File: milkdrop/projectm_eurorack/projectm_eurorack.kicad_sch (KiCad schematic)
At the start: 59 parts, among them J1 Micro_SD_Card, J2 Barrel_Jack_Switch, J2 Conn_02x05_Odd_Even, J3 AudioJack3_SwitchT, J4 USB_A, J5 AudioJack3_SwitchT, J6 690-019-298-412, Q1 MMBT3904, SW1 SW_Push, U1 RT9742SNGV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

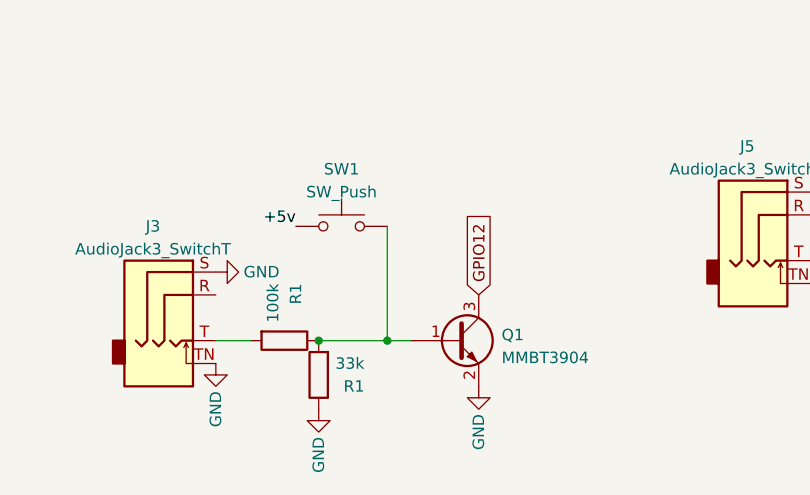
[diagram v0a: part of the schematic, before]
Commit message: Added missing base resistor
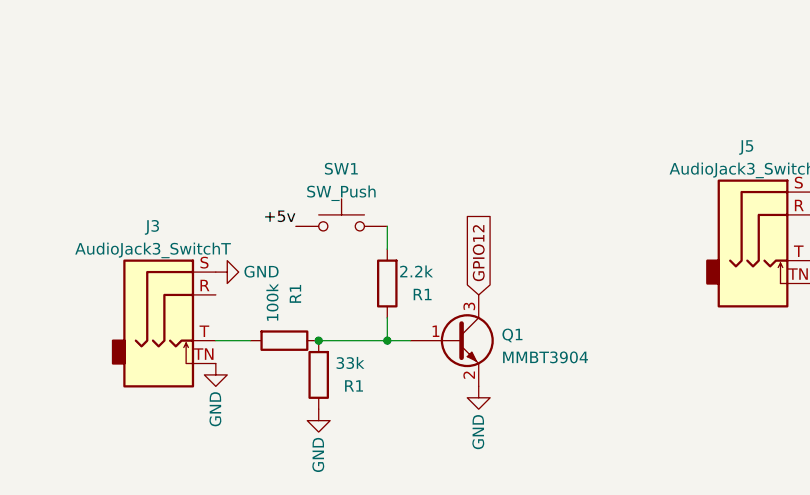
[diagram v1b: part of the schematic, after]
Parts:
- added R1: 2.2k, Resistor_SMD:R_0603_1608Metric, symbol Device:R
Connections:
- net at Q1.1 (B), R1.1, R1.2: now also R1.1; no longer SW1.2
- new net: R1.2, SW1.2
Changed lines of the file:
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@@
   (junction (at 440.69 314.96) (diameter 0) (color 0 0 0 0)
   )
+  (junction (at 373.38 328.93) (diameter 0) (color 0 0 0 0)
+  )
   (junction (at 554.99 275.59) (diameter 0) (color 0 0 0 0)
   )
@@
   (junction (at 369.824 157.48) (diameter 0) (color 0 0 0 0)
   )
-  (junction (at 373.38 328.93) (diameter 0) (color 0 0 0 0)
-  )
   (junction (at 71.374 109.22) (diameter 1.016) (color 0 0 0 0)
   )
@@
   (no_connect (at 73.66 60.96))
   (no_connect (at 373.38 142.24))
+  (wire (pts (xy 373.38 328.93) (xy 375.92 328.93))
+    (stroke (width 0) (type default))
+  )
   (wire (pts (xy 431.8 320.04) (xy 445.77 320.04))
     (stroke (width 0) (type default))
@@
     (stroke (width 0) (type solid))
   )
-  (wire (pts (xy 373.38 328.93) (xy 375.92 328.93))
-    (stroke (width 0) (type default))
-  )
   (wire (pts (xy 486.41 273.05) (xy 486.41 275.59))
     (stroke (width 0) (type default))
@@
     (stroke (width 0) (type solid))
   )
+  (wire (pts (xy 373.38 326.39) (xy 373.38 328.93))
+    (stroke (width 0) (type default))
+  )
   (wire (pts (xy 544.83 162.56) (xy 544.83 163.83))
     (stroke (width 0) (type solid))
@@
     (stroke (width 0) (type solid))
   )
+  (wire (pts (xy 373.38 316.23) (xy 373.38 318.77))
+    (stroke (width 0) (type default))
+  )
   (wire (pts (xy 67.564 81.28) (xy 73.66 81.28))
     (stroke (width 0) (type solid))
@@
     (stroke (width 0) (type solid))
   )
-  (wire (pts (xy 373.38 316.23) (xy 373.38 328.93))
-    (stroke (width 0) (type default))
-  )
   (wire (pts (xy 455.93 326.39) (xy 455.93 327.66))
     (stroke (width 0) (type default))
@@
         )
       )
+    )
+  )
+  (symbol (lib_id "Device:R") (at 373.38 322.58 180) (unit 1)
+    (in_bom yes) (on_board yes) (dnp no)
+    (property "Reference" "R1" (at 378.46 323.85 0)
+      (effects (font (size 1.27 1.27)) (justify left))
+    )
+    (property "Value" "2.2k" (at 378.46 321.31 0)
+      (effects (font (size 1.27 1.27)) (justify left))
+    )
+    (property "Footprint" "Resistor_SMD:R_0603_1608Metric" (at 375.158 322.58 90)
+      (effects (font (size 1.27 1.27)) hide)
+    )
+    (property "Datasheet" "~" (at 373.38 322.58 0)
+      (effects (font (size 1.27 1.27)) hide)
+    )
+    (property "Manufacturer" "Yageo" (at 373.38 322.58 0)
+      (effects (font (size 1.27 1.27)) hide)
+    )
+    (property "MPN" "RC0603FR-075K1L" (at 373.38 322.58 0)
+      (effects (font (size 1.27 1.27)) hide)
+    )
+    (property "Digi-Key_PN" "311-5.10KHRCT-ND" (at 373.38 322.58 0)
+      (effects (font (size 1.27 1.27)) hide)
+    )
+    (pin "1")
+    (pin "2")
+    (instances
+      (project "rpi-cm4-base-carrier"
+        (path "/33dfa1ae-775d-4f59-9fac-fe3d1ea5f9b0/fc4c71a5-1008-4ac4-98db-57c838c57d91"
+          (reference "R1") (unit 1)
+        )
+      )
+      (project "F8_tracker"
+        (path "/573bef89-e314-4649-a237-4312f807e0bf"
+          (reference "R22") (unit 1)
+        )
+      )
+      (project "projectm_eurorack"
+        (path "/b95ea5db-d646-4f7a-a27d-ad50ef54e923"
+          (reference "R12") (unit 1)
+        )
+      )
